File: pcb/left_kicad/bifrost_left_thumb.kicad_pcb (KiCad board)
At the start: 2 copper layers, 57.8 x 36.4 mm, 5 parts, among them SW41 UNASSIGNED_41, SW42 UNASSIGNED_42, SW43 UNASSIGNED_43

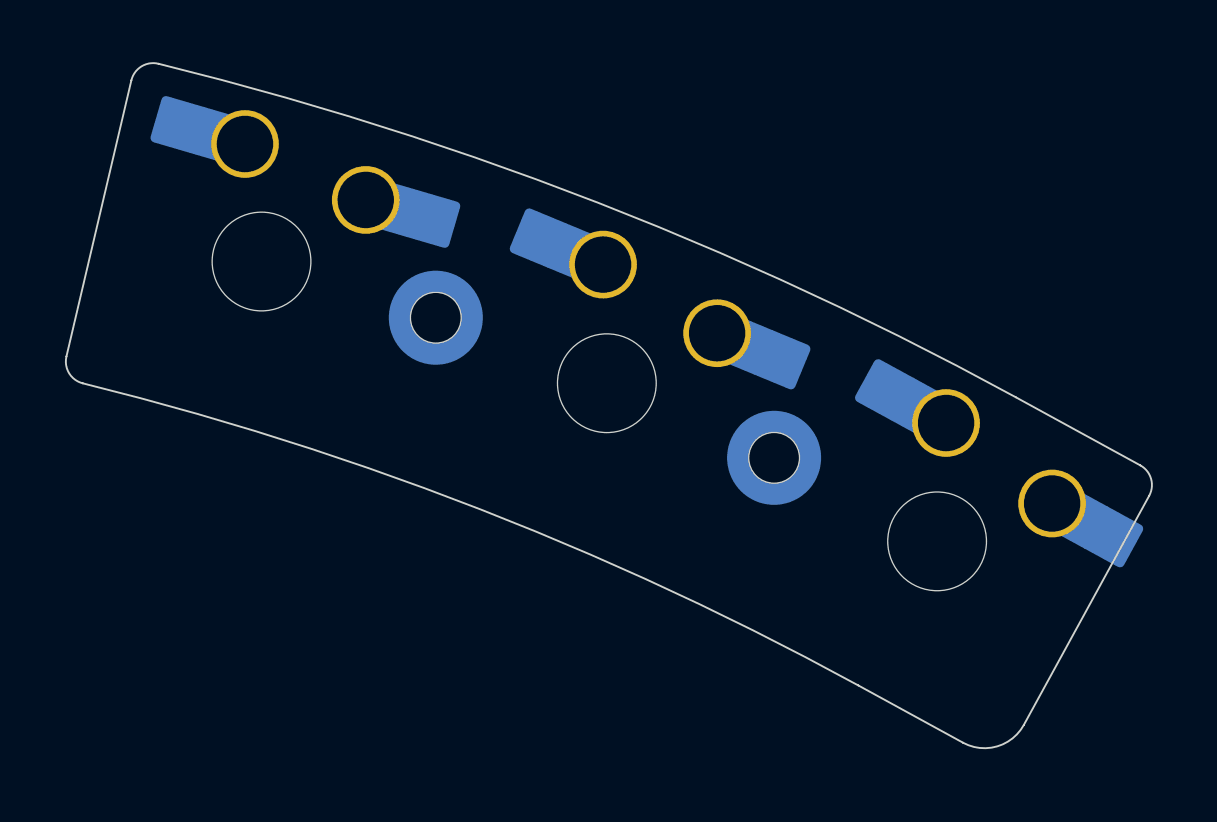
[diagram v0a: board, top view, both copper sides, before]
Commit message: Update KiCad keyboard designs
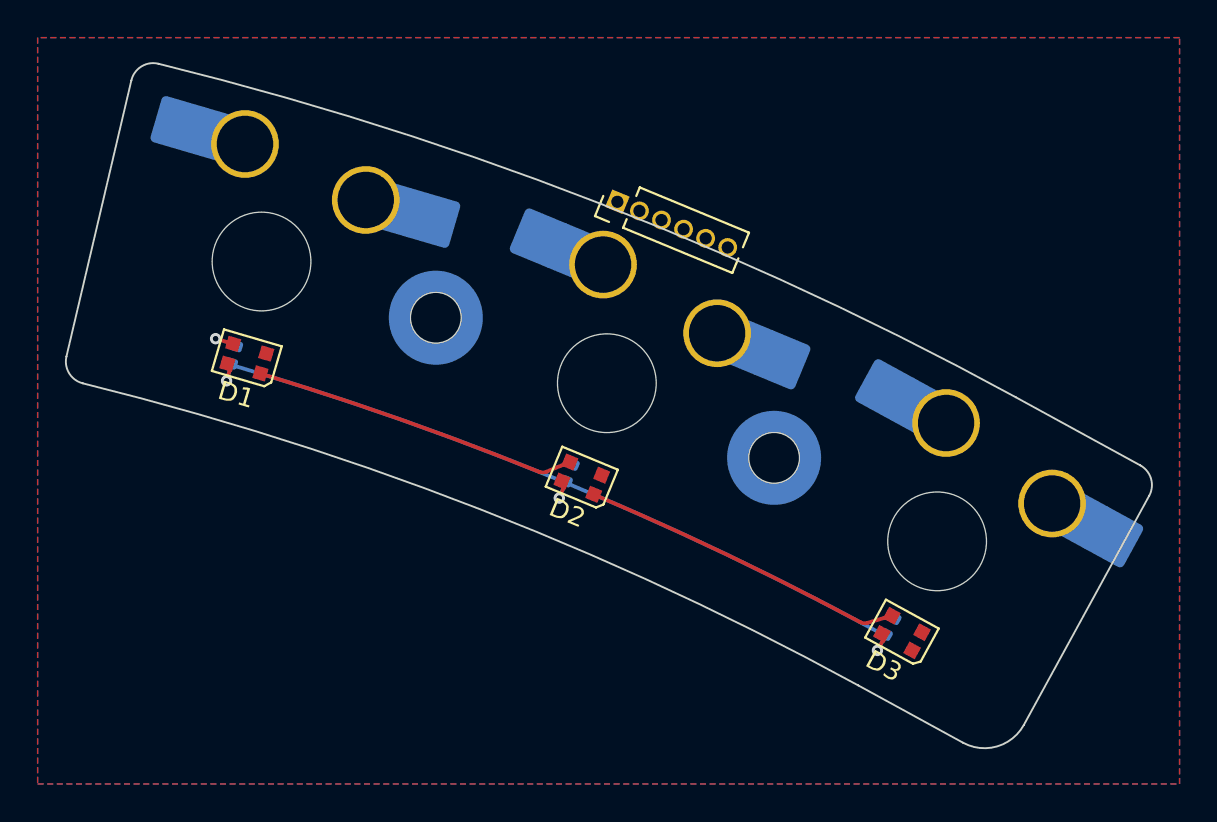
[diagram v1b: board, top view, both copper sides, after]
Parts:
- added C1: 100n, Capacitor_SMD:C_0402_1005Metric, B.Cu at (73.1, 71.8)
- added C2: 100n, Capacitor_SMD:C_0402_1005Metric, B.Cu at (91.0, 78.0)
- added C3: 100n, Capacitor_SMD:C_0402_1005Metric, B.Cu at (108.0, 86.2)
- added D1: WS2812B-2020, LED_SMD:LED_WS2812B-2020_PLCC4_2.0x2.0mm, F.Cu at (73.8, 72.0)
- added D2: WS2812B-2020, LED_SMD:LED_WS2812B-2020_PLCC4_2.0x2.0mm, F.Cu at (91.6, 78.3)
- added D3: WS2812B-2020, LED_SMD:LED_WS2812B-2020_PLCC4_2.0x2.0mm, F.Cu at (108.6, 86.6)
- added J1: Conn_01x06, Connector_PinHeader_1.27mm:PinHeader_1x06_P1.27mm_Vertical, F.Cu at (93.5, 63.6)
- renumbered SW41 to SW1, SW42 to SW2, SW43 to SW3
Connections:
- SW1 pad 1: unconnected-(SW41-Pad1) -> PIN_T1
- SW2 pad 1: unconnected-(SW42-Pad1) -> PIN_T2
- SW3 pad 1: unconnected-(SW43-Pad1) -> PIN_T3
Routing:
- net RGB_PWR: track 0.00 -> 43.5 mm, vias 0 -> 3
- net Net-(D2-DOUT): track 0.00 -> 17.5 mm
- net Net-(D1-DOUT): track 0.00 -> 17.5 mm
- net RGB: track 0.00 -> 1.23 mm, vias 0 -> 1
- added copper zone on B.Cu, net GND
- added copper zone on F.Cu, net GND

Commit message: Update PCB designs
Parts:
- J1: moved to B.Cu
- SW1: value UNASSIGNED_41 -> 1U
- SW2: value UNASSIGNED_42 -> 1U
- SW3: value UNASSIGNED_43 -> 1U
- moved C1 57.7 mm to (120.0, 105.4), turned to 96.179 degrees
- moved D1 57.6 mm to (120.7, 105.3), turned to -173.821 degrees
- moved SW1 56.0 mm to (119.5, 100.3), turned to 6.179 degrees
- moved C2 54.7 mm to (138.9, 104.4), turned to 90 degrees
- moved D2 54.6 mm to (139.6, 104.4), turned to 180 degrees
- moved H1 54.2 mm to (129.2, 99.5), turned to -157.5 degrees
- moved C3 53.3 mm to (157.8, 105.4), turned to 83.821 degrees
- moved D3 53.3 mm to (158.5, 105.5), turned to 173.821 degrees
- moved SW2 52.8 mm to (138.9, 99.2), turned to 0 degrees
- moved H2 51.8 mm to (148.6, 99.5), turned to -157.5 degrees
- moved SW3 51.3 mm to (158.3, 100.3), turned to -6.179 degrees
- moved J1 49.8 mm to (135.7, 90.1), turned to -90 degrees
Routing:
- net RGB_PWR: track 43.5 -> 73.7 mm
- net RGB: track 1.23 -> 28.9 mm, vias 1 -> 0
- net PIN_T3: track 0.00 -> 24.2 mm
- net PIN_T1: track 0.00 -> 17.4 mm
- net PIN_T2: track 0.00 -> 5.41 mm
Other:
- board size 57.8 x 36.4 mm -> 58.5 x 21 mm
